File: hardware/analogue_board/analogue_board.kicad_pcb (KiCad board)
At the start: 4 copper layers, 49.6 x 103 mm, 406 parts, among them J1001 TRS MIDI holes, J101 Spare GPIO, MIDI links, Pico 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, J201 Eurorack power 2x5 shrouded, J301 Audio in holes, J302 Audio out holes, J303 Codec RST, J401 CV jack holes, J601 Pot wiper holes; pot tops to 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, J602 Gate out holes, J603 Gate expansion: QH', SRCLK, R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, J701 Button / switch / encoder hol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, J702 Qwiic SM04B-SRSS-TB, J703 I2C holes for a wired display, J704 WS2812 chain holes, J801 Gate in holes, J802 Probe holes: PR1-10 100 kΩ, P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, J901 Edge strip, left, J902 Edge strip, right, Q201 AO3401A, U1001 SN74AHCT1G125DBVR, U1002 H11L1SR2M, U201 TPS54308DDCR, U202 L78M05ABDT-TR, U203 XC6206P332MR-G, U204 XC6206P332MR-G, U301 PCM3060PWR, U302 TL074HIDR, U401 ADS8688IDBTR, U402 DG412DQ-T1-E3, U403 DG412DQ-T1-E3, U501 DAC8568IAPWR, U502 TL074HIDR, U503 TL074HIDR, U504 TL074HIDR, U601 MCP3208-CI/SL, U602 74HCT595D, U701 TCA9555PWR, U702 M24C64-RMN6TP, U703 SN74AHCT1G125DBVR, U801 LM393DR2G, U802 LM393DR2G

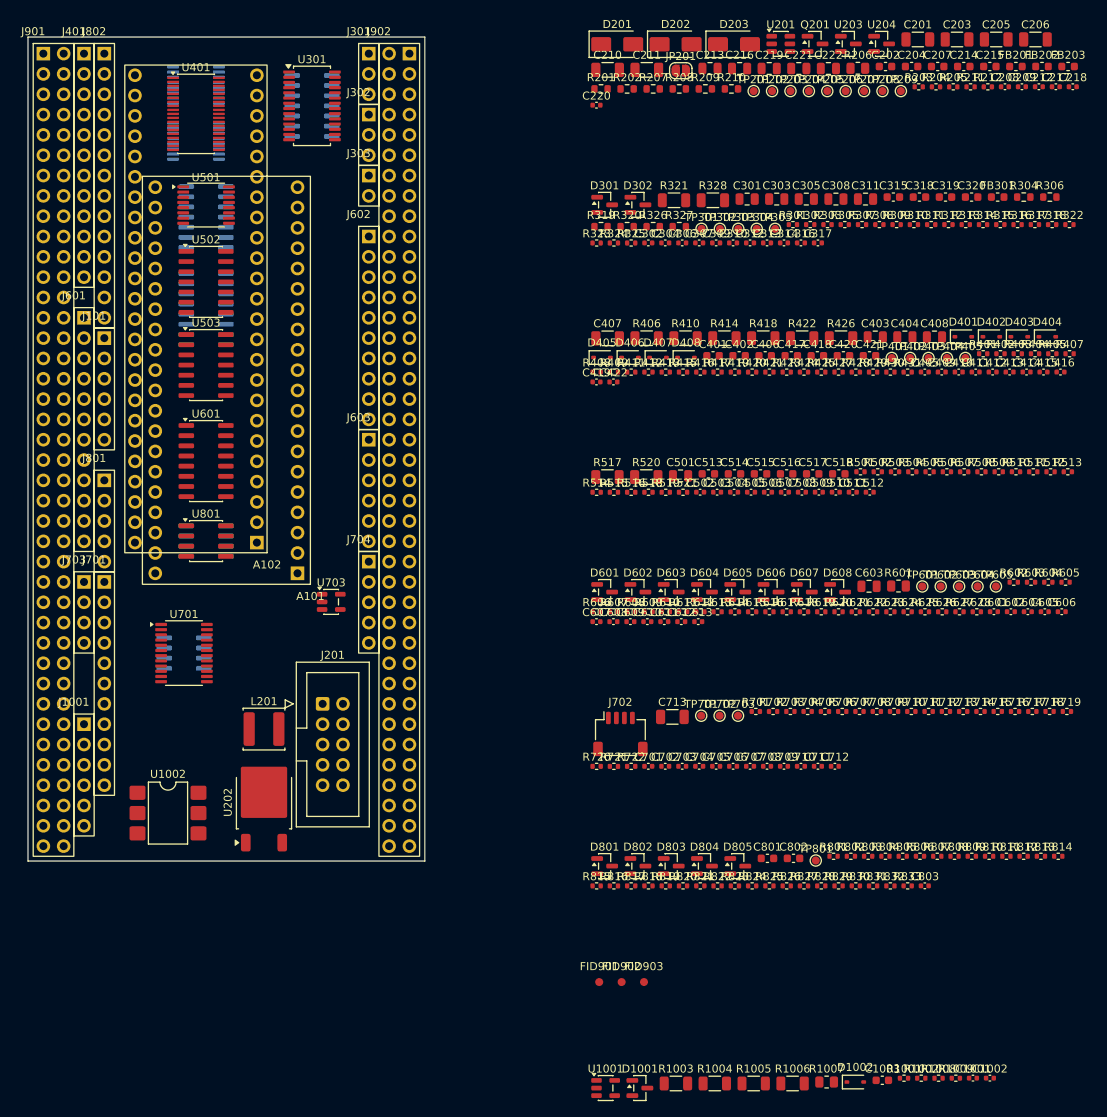
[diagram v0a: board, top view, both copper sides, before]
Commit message: Analogue board: first-pass placement; space reclaimed; four wiring banks
- autoplace.py places every unanchored part as close as it fits to the
  pins it connects to: decoupling capacitors at their pin, chains growing
  from their ICs, the buck's loop kept on one face. All 430 parts placed;
  DRC courtyards clean, schematic parity clean, heights checked (<= 2.5 mm
  under the modules, <= 8 mm in the USB keep-outs).
- Space reclaimed (David): Teensy socket without holes for its unused
  far-end pins 20-28 (headers 1x19 + 1x20); right strip (10HP only) without
  holes at 11-15 and 26-30, and outer hole only at 10, 16, 31. checks.py
  lets a project footprint omit only pins the netlist leaves unconnected.
- 74HCT595 in TSSOP-16 (74HCT595PW, C99710, same pinout) sideways in the
  right channel; vertical Qwiic socket (BM04B-SRSS-TB, C160390) below the
  modules, its cable straight up (the side-entry plug had no clear run).
- Wiring field as four mixed banks (David): each quarter of the board has
  some of every channel type, 50/50 left and right, jack-detect holes
  beside their inputs; wiring.py holds the plan, schematic and placement
  both read it. 94 holes.
- Reference designators off the silkscreen for passives and hole groups.

Co-Authored-By: Claude Opus 5.5 <noreply@anthropic.com>
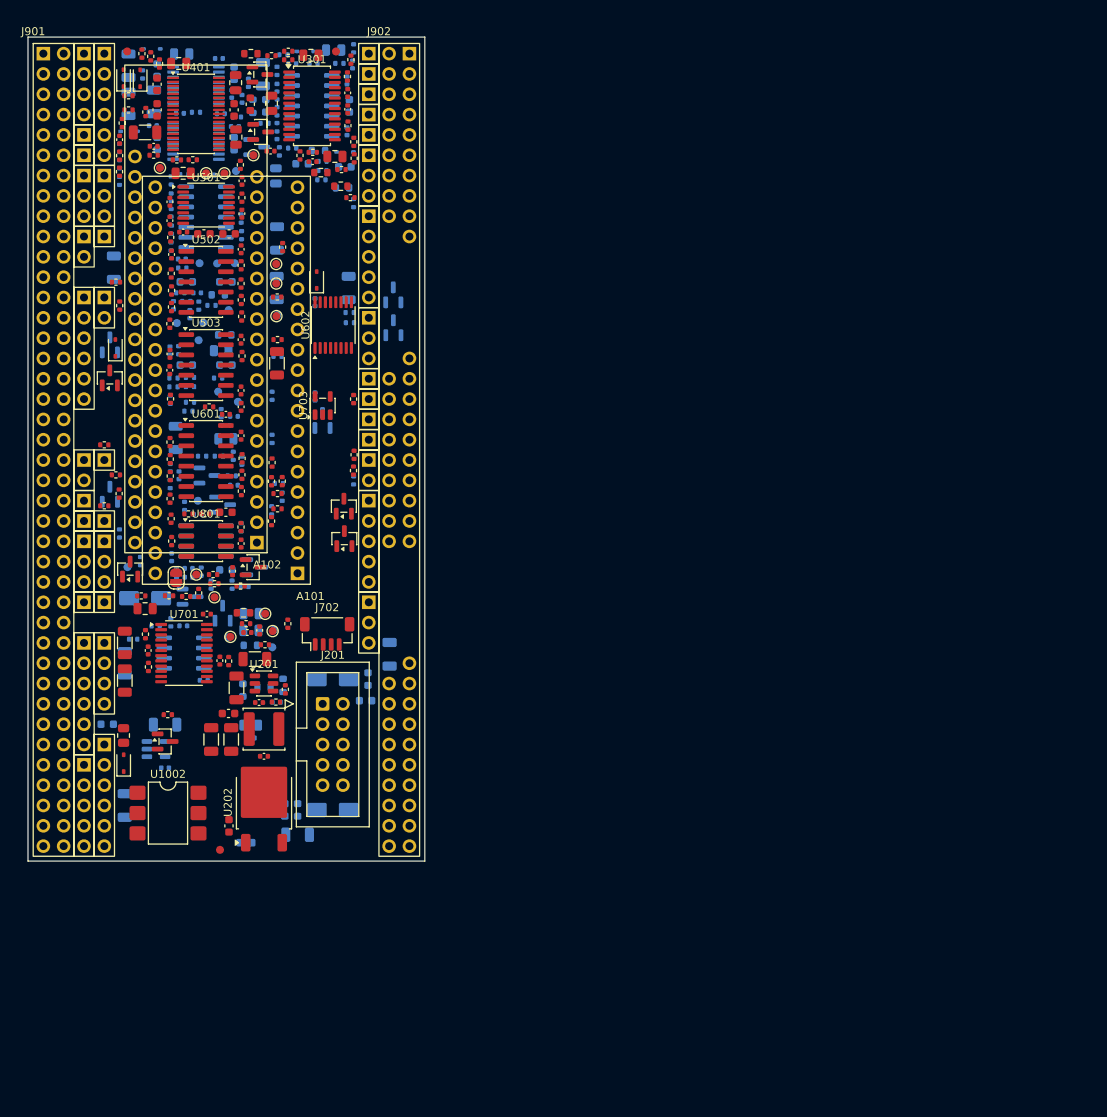
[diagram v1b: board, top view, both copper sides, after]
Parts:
- removed J301: Audio in holes, analogue_board:WiringHoles_1x03
- removed J302: Audio out holes, analogue_board:WiringHoles_1x03
- removed J401: CV jack holes, analogue_board:WiringHoles_1x12
- removed J601: Pot wiper holes; pot tops to POT_REF, analogue_board:WiringHoles_1x12
- removed J602: Gate out holes, analogue_board:WiringHoles_1x10
- removed J701: Button / switch / encoder holes, analogue_board:WiringHoles_1x11
- removed J801: Gate in holes, analogue_board:WiringHoles_1x05
- removed J802: Probe holes: PR1-10 100 kΩ, PR11-14 22 kΩ, analogue_board:WiringHoles_1x14
- added J310: Holes, left top, analogue_board:WiringHoles_1x01, F.Cu at (37.0, 42.2)
- added J311: Holes, left bottom, analogue_board:WiringHoles_1x01, F.Cu at (37.0, 88.0)
- added J312: Holes, right top, analogue_board:WiringHoles_1x01, F.Cu at (72.6, 42.2)
- added J313: Holes, right middle, analogue_board:WiringHoles_1x01, F.Cu at (72.6, 80.3)
- added J410: Holes, left top, analogue_board:WiringHoles_1x04, F.Cu at (37.0, 32.1)
- added J411: Holes, left bottom, analogue_board:WiringHoles_1x02, F.Cu at (37.0, 82.9)
- added J412: Holes, right top, analogue_board:WiringHoles_1x01, F.Cu at (72.6, 32.1)
- added J413: Holes, right top, analogue_board:WiringHoles_1x01, F.Cu at (72.6, 37.1)
- added J414: Holes, right middle, analogue_board:WiringHoles_1x01, F.Cu at (72.6, 72.7)
- added J415: Holes, right middle, analogue_board:WiringHoles_1x01, F.Cu at (72.6, 77.8)
- added J610: Holes, left top, analogue_board:WiringHoles_1x03, F.Cu at (37.0, 47.3)
- added J611: Holes, left bottom, analogue_board:WiringHoles_1x03, F.Cu at (37.0, 93.0)
- added J612: Holes, left top, analogue_board:WiringHoles_1x03, F.Cu at (39.5, 47.3)
- added J613: Holes, left bottom, analogue_board:WiringHoles_1x03, F.Cu at (39.5, 93.0)
- added J614: Holes, right top, analogue_board:WiringHoles_1x05, F.Cu at (72.6, 52.4)
- added J615: Holes, right middle, analogue_board:WiringHoles_1x05, F.Cu at (72.6, 88.0)
- added J710: Holes, left top, analogue_board:WiringHoles_1x02, F.Cu at (37.0, 54.9)
- added J711: Holes, left bottom, analogue_board:WiringHoles_1x01, F.Cu at (37.0, 100.7)
- added J712: Holes, left top, analogue_board:WiringHoles_1x01, F.Cu at (39.5, 54.9)
- added J713: Holes, left bottom, analogue_board:WiringHoles_1x01, F.Cu at (39.5, 100.7)
- added J714: Holes, right top, analogue_board:WiringHoles_1x03, F.Cu at (72.6, 65.1)
- added J715: Holes, right middle, analogue_board:WiringHoles_1x03, F.Cu at (72.6, 100.7)
- added J810: Holes, left top, analogue_board:WiringHoles_1x01, F.Cu at (37.0, 44.8)
- added J811: Holes, left bottom, analogue_board:WiringHoles_1x01, F.Cu at (37.0, 90.5)
- added J812: Holes, left top, analogue_board:WiringHoles_1x06, F.Cu at (39.5, 32.1)
- added J813: Holes, left bottom, analogue_board:WiringHoles_1x01, F.Cu at (39.5, 82.9)
- added J814: Holes, left bottom, analogue_board:WiringHoles_1x01, F.Cu at (39.5, 90.5)
- added J815: Holes, right top, analogue_board:WiringHoles_1x01, F.Cu at (72.6, 34.6)
- added J816: Holes, right top, analogue_board:WiringHoles_1x01, F.Cu at (72.6, 39.7)
- added J817: Holes, right top, analogue_board:WiringHoles_1x03, F.Cu at (72.6, 44.8)
- added J818: Holes, right middle, analogue_board:WiringHoles_1x01, F.Cu at (72.6, 75.2)
- added J819: Holes, right middle, analogue_board:WiringHoles_1x02, F.Cu at (72.6, 82.9)
- C1001, C1002, C1003, C201, C202, C203, C204, C209, C213, C214, C216, C217, C219, C221, C304, C307, C308, C309, C310, C311, C312, C313, C314, C315, C316, C318, C319, C320, C405, C407, C409, C411, C412, C413, C416, C417, C418, C419, C420, C421, C422, C502, C509, C510, C513, C514, C515, C516, C602, C603, C607, C608, C610, C611, C613, C702, C703, C704, C706, C708, C711, C712, C713, C802, D201, D202, D203, D404, D405, D407, D408, D601, D603, D604, D605, D606, D801, D803, D804, D805, FB201, FB202, FB203, R1001, R1002, R1003, R1006, R201, R202, R205, R206, R207, R208, R210, R211, R304, R305, R307, R308, R309, R311, R312, R314, R315, R317, R318, R319, R321, R325, R326, R328, R402, R403, R406, R407, R411, R413, R414, R415, R417, R418, R419, R422, R423, R426, R427, R430, R431, R502, R503, R504, R506, R508, R510, R512, R514, R515, R516, R517, R518, R519, R601, R604, R606, R610, R613, R614, R620, R623, R624, R625, R626, R701, R703, R705, R710, R711, R714, R715, R722, R806, R809, R810, R811, R812, R813, R814, R815, R816, R822, R823, R826, R830, R832, R833, TP204, TP205, TP207, TP208, TP209, TP301, TP302, TP303, TP304, TP403, TP405, TP601, TP603, TP604, TP703, TP801, U1001, U203, U204: moved to B.Cu
- J702: value Qwiic SM04B-SRSS-TB -> Qwiic BM04B-SRSS-TB; footprint Connector_JST:JST_SH_SM04B-SRSS-TB_1x04-1MP_P1.00mm_Horizontal -> Connector_JST:JST_SH_BM04B-SRSS-TB_1x04-1MP_P1.00mm_Vertical
- U602: value 74HCT595D -> 74HCT595PW; footprint Package_SO:SOIC-16_3.9x9.9mm_P1.27mm -> Package_SO:TSSOP-16_4.4x5mm_P0.65mm; moved to F.Cu
- moved C215 134.4 mm to (55.1, 128.6), turned to 90 degrees
- moved C217 132.8 mm to (59.5, 124.8)
- moved C214 132.2 mm to (57.2, 130.7)
- moved FID901 130.4 mm to (42.4, 31.8)
- moved FB203 129.3 mm to (56.9, 111.6), turned to 90 degrees
- moved FB201 129.2 mm to (63.7, 126.6), turned to 90 degrees
- moved C212 128.0 mm to (59.5, 119.9)
- moved R830 127.4 mm to (41.4, 48.0), turned to 90 degrees
- moved C209 126.2 mm to (57.8, 117.6)
- moved C201 126.1 mm to (63.7, 129.7)
- moved C205 124.9 mm to (56.1, 111.3), turned to 90 degrees
- moved C206 124.6 mm to (58.4, 107.8)
- moved R821 124.4 mm to (45.3, 32.4), turned to 90 degrees
- moved R820 124.1 mm to (44.2, 32.1), turned to 90 degrees
- moved R605 123.2 mm to (41.5, 63.6), turned to 90 degrees
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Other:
- board text removed: "not yet placed: CV DAC"
- board text removed: "not yet placed: CV jacks & ADC"
- board text removed: "not yet placed: Codec & audio"
- board text removed: "not yet placed: Edge strips"
- board text removed: "not yet placed: Expander, I2C & LEDs"
- board text removed: "not yet placed: Gate ins & jack detect"
- board text removed: "not yet placed: Pots & gate outs"
- board text removed: "not yet placed: Power"
- board text removed: "not yet placed: TRS MIDI"

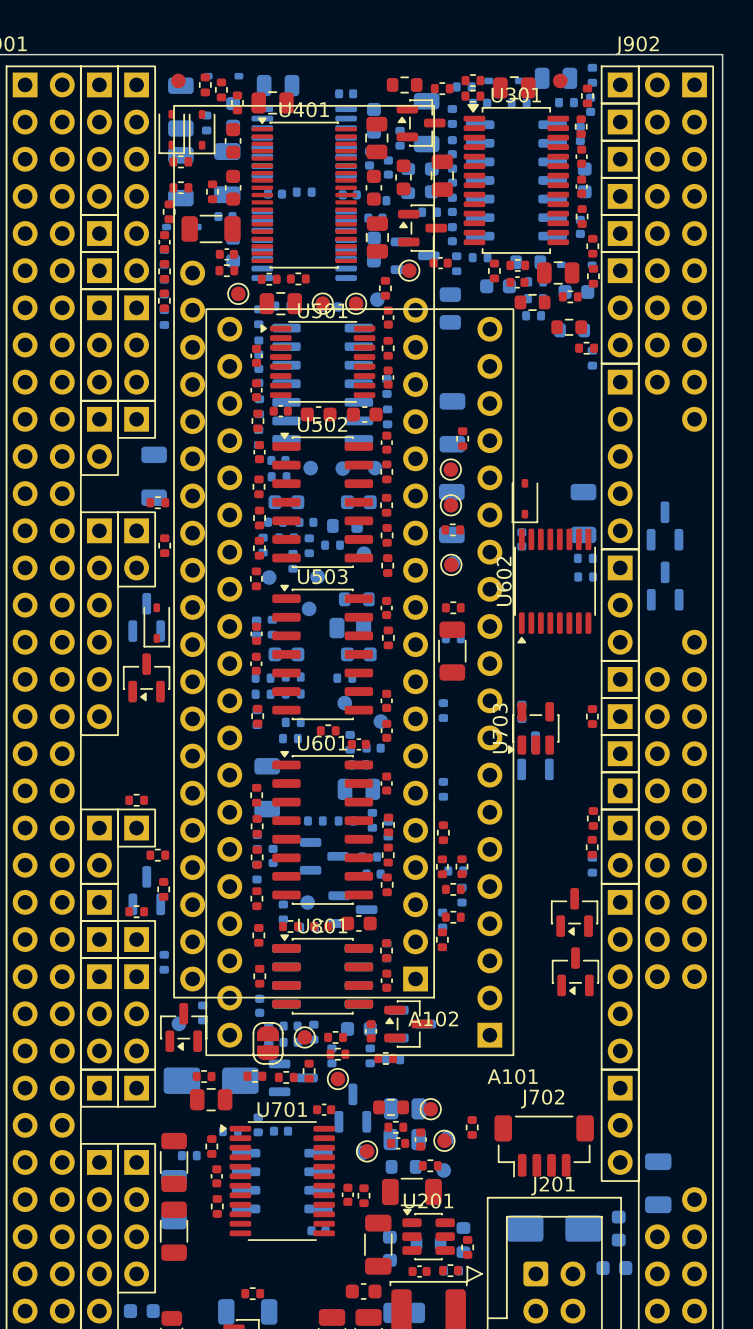
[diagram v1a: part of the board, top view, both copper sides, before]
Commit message: Analogue board: bus chips level with their module pins; design rules; trial autoroute
Re-floorplan the centre channel in the order of the module's buses (SPI-A,
SPI-B, I2S, I2C), so the codec is 6 mm from the Pico's I2S pins instead of
38 mm; CV output op-amps move to the top-right corner.

Net classes (0.15/0.15 default, 0.3 power) and an In1 ground plane are
written into the project. autoroute.py runs Freerouting on a copy of the
board to measure routability. Schematic hole groups no longer overlap.

Co-Authored-By: Claude Opus 5.5 <noreply@anthropic.com>
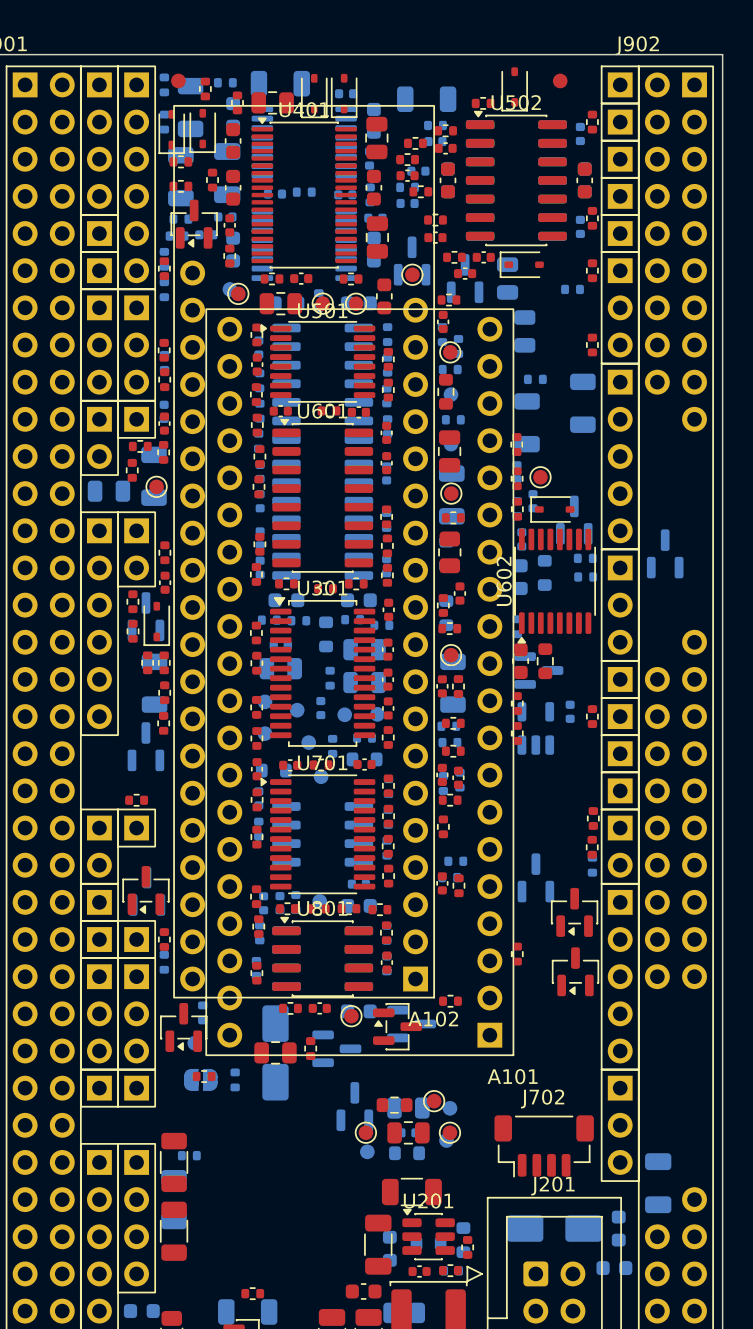
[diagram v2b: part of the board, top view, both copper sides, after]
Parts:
- C213, C318, C409, C411, C513, C514, C602, C603, C607, C608, C610, C611, C702, C703, C708, D404, D405, D407, D408, D603, D801, R208, R305, R307, R314, R315, R317, R325, R402, R407, R417, R419, R427, R430, R502, R503, R508, R514, R519, R601, R604, R606, R610, R613, R614, R623, R624, R701, R705, R714, R722, R822, R826, R832, TP204, TP207, TP403, TP405, TP601, TP801: moved to F.Cu
- C220, C301, C303, C305, C317, C410, C415, C511, C512, C517, C518, C606, C609, C705, C801, D301, D602, D802, JP201, R212, R303, R306, R313, R316, R320, R322, R323, R409, R410, R428, R429, R513, R520, R521, R611, R612, R622, R707, R719, R820, R821, TP201, TP206, TP305, TP605, TP701, U503, U703: moved to B.Cu
- moved R303 46.5 mm to (55.1, 76.7), turned to 0 degrees
- moved R306 46.2 mm to (55.1, 78.2)
- moved R301 45.6 mm to (40.3, 71.6), turned to 90 degrees
- moved R302 42.7 mm to (39.3, 69.4), turned to 90 degrees
- moved R304 41.3 mm to (48.9, 78.9), turned to 0 degrees
- moved C511 40.9 mm to (69.9, 35.4)
- moved C301 39.7 mm to (55.1, 70.7)
- moved C302 36.2 mm to (56.7, 70.7)
- moved C306 36.2 mm to (56.7, 72.7)
- moved U301 36.2 mm to (52.3, 72.3)
- moved C516 35.9 mm to (70.2, 38.6), turned to 90 degrees
- moved C303 35.5 mm to (49.4, 72.0), turned to 0 degrees
- moved U503 35.0 mm to (65.5, 38.6)
- moved R314 34.7 mm to (54.6, 66.2)
- moved C515 34.2 mm to (60.8, 38.6), turned to 90 degrees
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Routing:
- added copper zone on In1.Cu, net GND
